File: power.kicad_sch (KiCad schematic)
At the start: 47 parts, among them SW2 SW_DPST

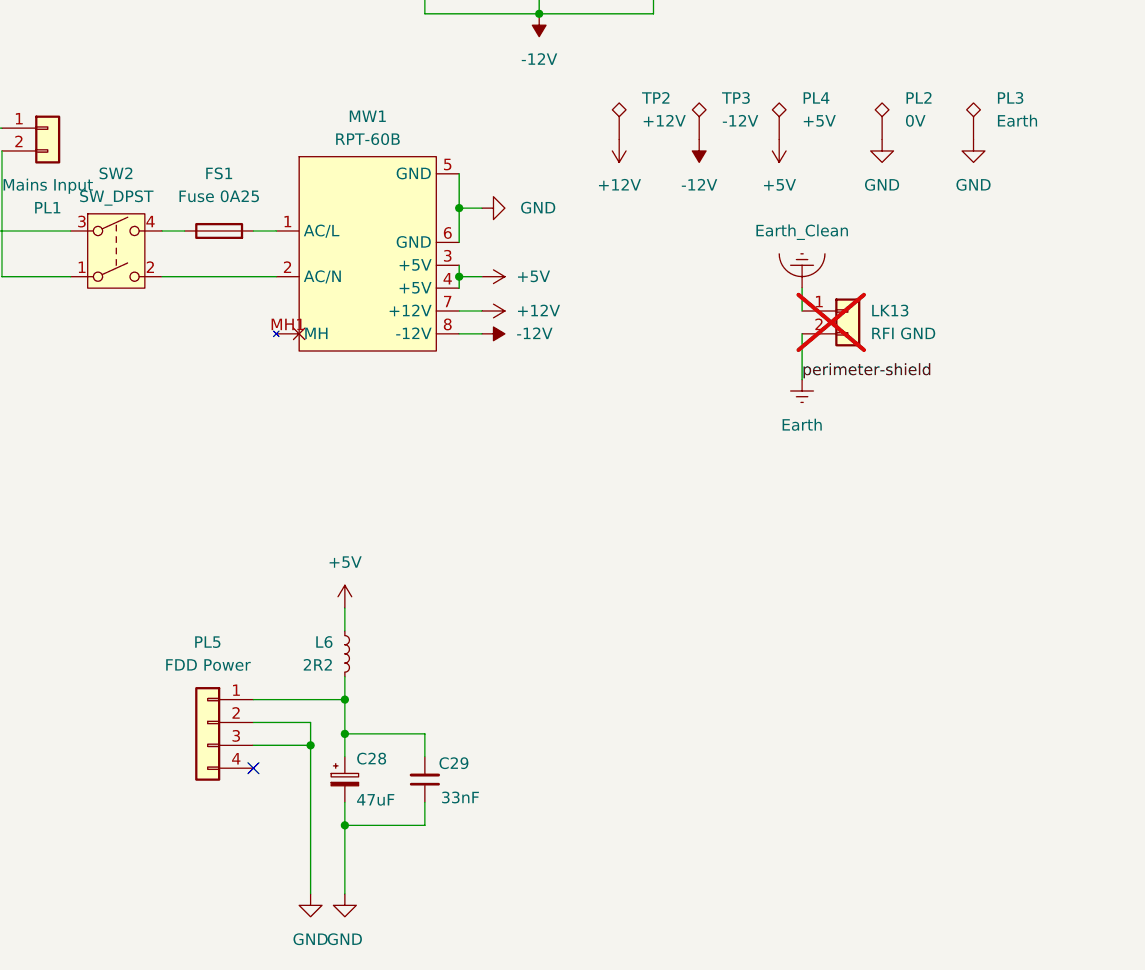
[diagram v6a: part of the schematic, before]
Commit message: complete routing
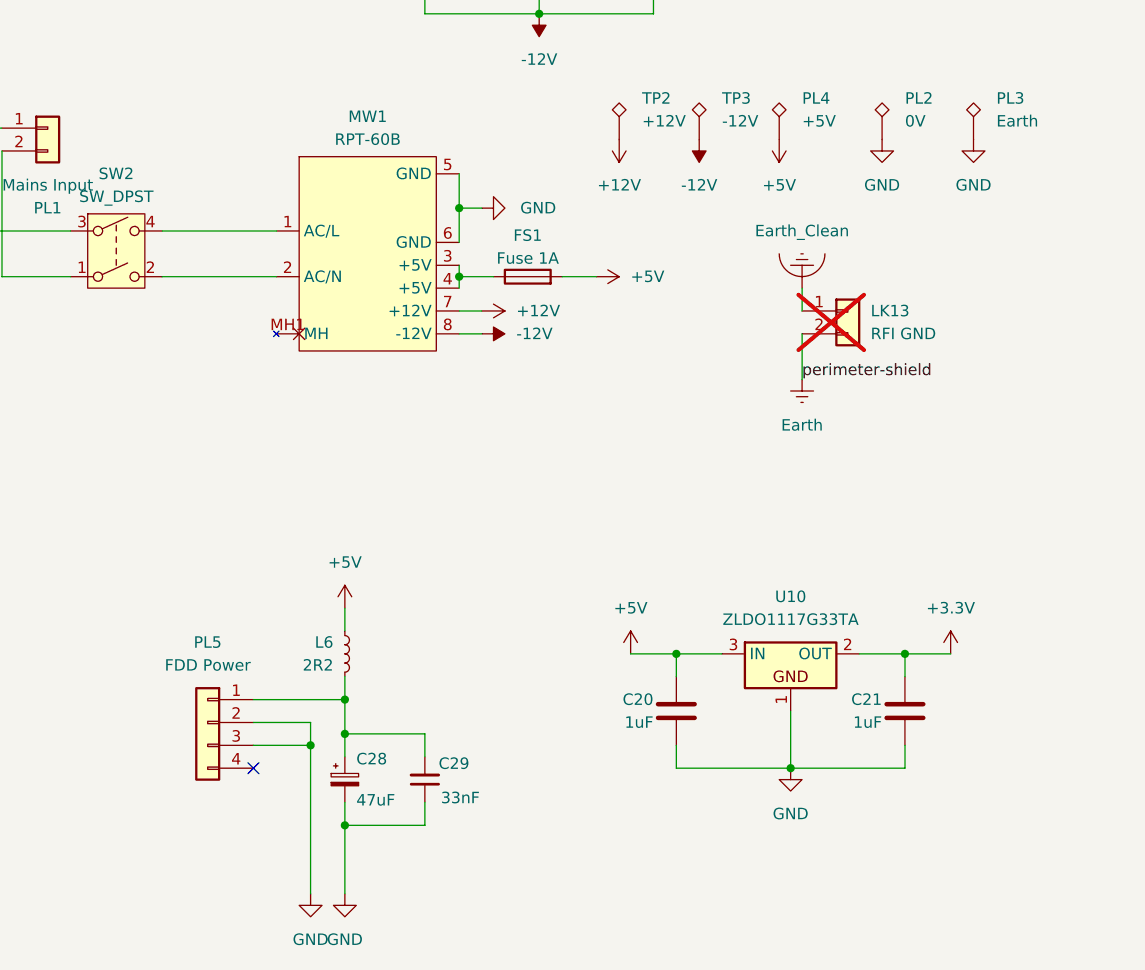
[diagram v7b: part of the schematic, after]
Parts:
- added C20, C21: 1uF, Capacitor_SMD:C_0805_2012Metric, symbol Device:C
- added U10: ZLDO1117G33TA, PCM_Package_TO_SOT_SMD_AKL:SOT-223-3_TabPin2, symbol PCM_Voltage_Regulator_AKL:ZLDO1117G33TA
- FS1: value Fuse 0A25 -> Fuse 1A
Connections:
- net +5V: now also FS1.2, C20.1, U10.3 (IN); no longer MW1.3 (+5V), MW1.4 (+5V)
- net GND: now also C20.2, C21.2, U10.1
- net at FS1.1: now also MW1.3 (+5V), MW1.4 (+5V); no longer SW2.4
- net at MW1.1 (AC/L): now also SW2.4; no longer FS1.2
- new net +3.3V: C21.1, U10.2 (OUT)
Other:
- moved on the sheet: FS1
